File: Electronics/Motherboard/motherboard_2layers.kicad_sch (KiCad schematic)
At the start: 54 parts, among them J1 DX07S024JJ3R1300, J2 Conn_02x10_Odd_Even, M1 AO3400A, M2 AO3400A, M3 AO3400A, U1 AMS1117-3.3, U2 TMC2209_SILENTSTEPSTICK, U3 TMC2209_SILENTSTEPSTICK, U4 TMC2209_SILENTSTEPSTICK, U5 TMC2209_SILENTSTEPSTICK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

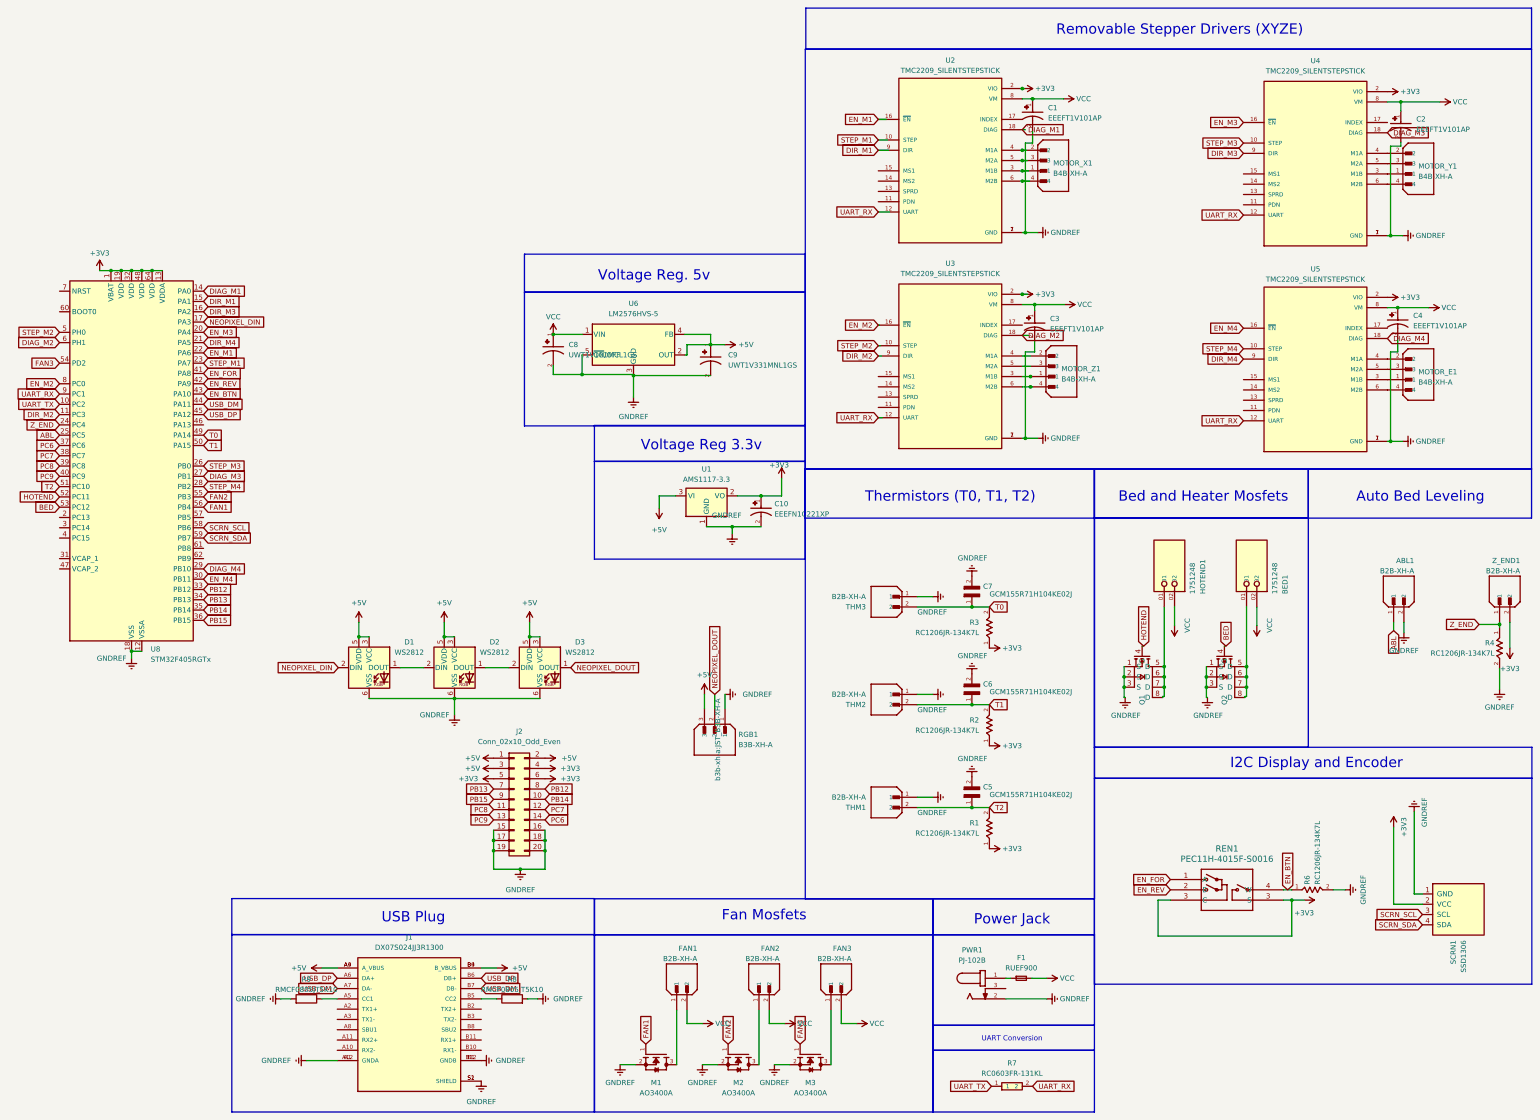
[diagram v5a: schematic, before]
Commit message: updated schmentic with proper values and updated usb c connector
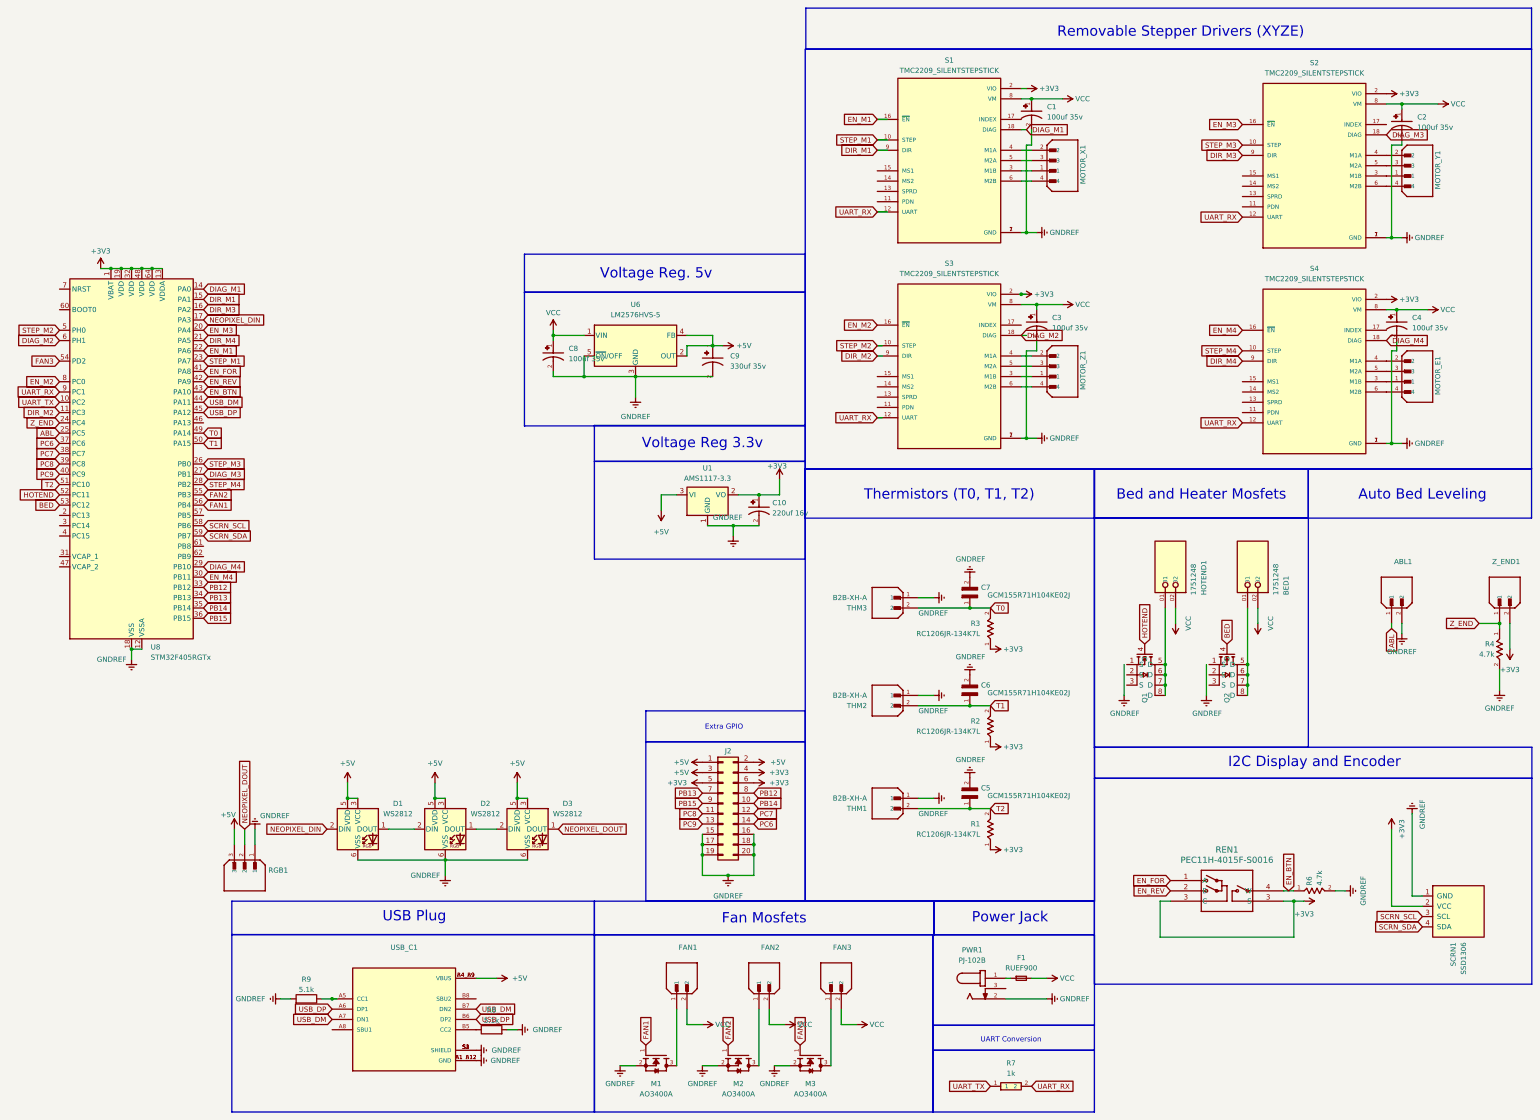
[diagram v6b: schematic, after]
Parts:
- removed C8: UWT1V101MCL1GS, UWT1V101MCL1GS:CAPAE830X1000N, symbol UWT1V101MCL1GS:UWT1V101MCL1GS
- removed J1: DX07S024JJ3R1300, DX07S024JJ3R1300:JAE_DX07S024JJ3R1300, symbol DX07S024JJ3R1300:DX07S024JJ3R1300
- added C8: 100uf 35v, CAP_EEEFT1V101AP, symbol EEEFT1V101AP:EEEFT1V101AP
- added USB_C1: TYPE-C-31-M-12, Connector_USB:USB_C_Receptacle_HRO_TYPE-C-31-M-12, symbol USB_C_Receptacle_HRO_TYPE:TYPE-C-31-M-12
- ABL1, FAN2, FAN3, Z_END1: Check_prices https://www.snapeda.com/parts/B2B-XH-A/JST+Sales+America+In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 -> (none); DigiKey_Part_Number 455-B2B-XH-A-ND -> (none); MANUFACTURER JST Sales America Inc. -> (none); MAXIMUM_PACKAGE_HEIGHT 7 mm -> (none); MF JST Sales -> (none); MP B2B-XH-A -> (none); PARTREV N/A -> (none); Package None -> (none); STANDARD Manufacturer Recommendations -> (none); SnapEDA_Link https://www.snapeda.com/parts/B2B-XH-A/JST+Sales+America+In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 -> (none)
- C1, C2, C3, C4: value EEEFT1V101AP -> 100uf 35v; Availability In Stock -> (none); Check_prices https://www.snapeda.com/parts/EEEFT1V101AP/Panasonic/view-p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 -> (none); Description_1 100µF 35V Aluminum Electrolytic Capacitors Radial, Can - SM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 -> (none); MANUFACTURER Panasonic -> (none); MAXIMUM_PACKAGE_HEIGHT 5.8mm -> (none); MF Panasonic -> (none); MP EEEFT1V101AP -> (none); PARTREV 10-Oct-19 -> (none); Package RADIAL-2 Panasonic -> (none); Price None -> (none); Purchase-URL https://www.snapeda.com/api/url_track_click_mouser/?unipart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 -> (none); STANDARD Manufacturer Recommendations -> (none); SnapEDA_Link https://www.snapeda.com/parts/EEEFT1V101AP/Panasonic/view-p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 -> (none)
- C10: value EEEFN1C221XP -> 220uf 16v; Availability In Stock -> (none); Check_prices https://www.snapeda.com/parts/EEE-FN1C221XP/Panasonic/view-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 -> (none); Description_1 Capacitor,16VDC, 220uF,SMD'Electrolytic | Panasonic Electro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 -> (none); MANUFACTURER Panasonic -> (none); MAXIMUM_PACKAGE_HEIGHT 7.7mm -> (none); MF Panasonic Electronic Components -> (none); MP EEE-FN1C221XP -> (none); PARTREV 10-Oct-19 -> (none); Package RADIAL-2 Panasonic -> (none); Price None -> (none); Purchase-URL https://www.snapeda.com/api/url_track_click_mouser/?unipart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 -> (none); STANDARD Manufacturer Recommendations -> (none); SnapEDA_Link https://www.snapeda.com/parts/EEE-FN1C221XP/Panasonic/view-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 -> (none)
- C9: value UWT1V331MNL1GS -> 330uf 35v; Availability In Stock -> (none); Check_prices https://www.snapeda.com/parts/UWT1V101MCL1GS/Nichicon/view-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 -> (none); Description_1 Capacitor Aluminum Electrolytic, 1000h 6.3 (Dia.) x 7.7mm, 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 -> (none); MANUFACTURER Nichicon -> (none); MAXIMUM_PACKAGE_HEIGHT 7.7mm -> (none); MF Nichicon -> (none); MP UWT1V101MCL1GS -> (none); PARTREV CAT.8100L -> (none); Package Radial Nichicon -> (none); Price None -> (none); Purchase-URL https://www.snapeda.com/api/url_track_click_mouser/?unipart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 -> (none); SNAPEDA_PN UWT1V101MCL1GS -> (none); STANDARD IPC-7351B -> (none); SnapEDA_Link https://www.snapeda.com/parts/UWT1V101MCL1GS/Nichicon/view-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 -> (none)
- FAN1: value B2B-XH-A -> ~
- MOTOR_E1, MOTOR_X1, MOTOR_Y1, MOTOR_Z1: Check_prices https://www.snapeda.com/parts/B4B-XH-A/JST+Sales+America+In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 -> (none); DigiKey_Part_Number 455-B4B-XH-A-ND -> (none); MANUFACTURER JST -> (none); MAXIMUM_PACKAGE_HEIGHT 7.00 mm -> (none); MF JST Sales -> (none); MP B4B-XH-A -> (none); PARTREV 7/4/21 -> (none); Package None -> (none); STANDARD Manufacturer Recommendations -> (none); SnapEDA_Link https://www.snapeda.com/parts/B4B-XH-A/JST+Sales+America+In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 -> (none)
- R4, R6: value RC1206JR-134K7L -> 4.7k; Check_prices https://www.snapeda.com/parts/RC1206JR-134K7L/Yageo/view-pa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 -> (none); DigiKey_Part_Number 13-RC1206JR-134K7LTR-ND -> (none); MANUFACTURER YAGEO -> (none); MF Yageo -> (none); MP RC1206JR-134K7L -> (none); Package SMD-2 Yageo -> (none); Purchase-URL https://www.snapeda.com/api/url_track_click_mouser/?unipart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 -> (none); SnapEDA_Link https://www.snapeda.com/parts/RC1206JR-134K7L/Yageo/view-pa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 -> (none)
- R7: value RC0603FR-131KL -> 1k; Check_prices https://www.snapeda.com/parts/RC0603FR-131KL/Yageo/view-par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 -> (none); DigiKey_Part_Number 13-RC0603FR-131KLTR-ND -> (none); MF Yageo -> (none); MP RC0603FR-131KL -> (none); Package 0603 Yageo -> (none); Purchase-URL https://www.snapeda.com/api/url_track_click_mouser/?unipart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 -> (none); SnapEDA_Link https://www.snapeda.com/parts/RC0603FR-131KL/Yageo/view-par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 -> (none)
- R8, R9: value RMCF0805JT5K10 -> 5.1k
- renumbered U2 to S1, U4 to S2, U3 to S3, U5 to S4
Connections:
- net +5V: now also USB_C1.A4_B9 (VBUS), USB_C1.B4_A9 (VBUS)
- net GNDREF: now also C8.2, USB_C1.A1_B12 (GND), USB_C1.B1_A12 (GND), USB_C1.S1 (SHIELD), USB_C1.S2 (SHIELD), USB_C1.S3 (SHIELD), USB_C1.S4 (SHIELD); no longer Q1.1 (S), Q1.2 (S), Q1.3 (S), Q2.1 (S), Q2.2 (S), Q2.3 (S)
- net USB_DM: now also USB_C1.A7 (DN1), USB_C1.B7 (DN2)
- net USB_DP: now also USB_C1.A6 (DP1), USB_C1.B6 (DP2)
- net VCC: now also C8.1
- net at R9.1: now also USB_C1.A5 (CC1)
- net at R8.1: now also USB_C1.B5 (CC2)
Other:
- note added: "Extra GPIO"
- moved on the sheet: ABL1, C10, C4, C5, C6, C7, C9, D1, D2, D3, J2, MOTOR_E1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

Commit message: more clean up neneds to be done
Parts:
- renumbered MOTOR_E1 to MOTOR_E, MOTOR_X1 to MOTOR_X, MOTOR_Y1 to MOTOR_Y, MOTOR_Z1 to MOTOR_Z
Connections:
- net GNDREF: now also Q1.1 (S), Q1.2 (S), Q1.3 (S), Q2.1 (S), Q2.2 (S), Q2.3 (S)
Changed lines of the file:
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@@
 	)
 	(junction
+		(at 328.295 179.07)
+		(diameter 0)
+		(color 0 0 0 0)
+	)
+	(junction
 		(at 203.2 218.44)
 		(diameter 0)
@@
 	)
 	(junction
+		(at 307.975 179.07)
+		(diameter 0)
+		(color 0 0 0 0)
+	)
+	(junction
 		(at 283.21 118.11)
 		(diameter 0)
@@
 	)
 	(junction
+		(at 307.975 176.53)
+		(diameter 0)
+		(color 0 0 0 0)
+	)
+	(junction
+		(at 328.295 176.53)
+		(diameter 0)
+		(color 0 0 0 0)
+	)
+	(junction
 		(at 349.25 232.41)
 		(diameter 0)
@@
 	(wire
 		(pts
+			(xy 307.34 179.07) (xy 307.975 179.07)
+		)
+		(stroke
+			(width 0)
+			(type default)
+		)
+	)
+	(wire
+		(pts
 			(xy 118.11 222.25) (xy 139.7 222.25)
 		)
@@
 	(wire
 		(pts
-			(xy 307.34 173.99) (xy 307.34 181.61)
-		)
-		(stroke
-			(width 0)
-			(type default)
-		)
-	)
-	(wire
-		(pts
 			(xy 283.21 96.52) (xy 283.21 118.11)
 		)
@@
 	(wire
 		(pts
-			(xy 327.66 173.99) (xy 327.66 181.61)
+			(xy 328.295 173.99) (xy 328.295 176.53)
 		)
 		(stroke
@@
 	(wire
 		(pts
+			(xy 328.295 179.07) (xy 327.66 179.07)
+		)
+		(stroke
+			(width 0)
+			(type default)
+		)
+	)
+	(wire
+		(pts
 			(xy 67.31 76.2) (xy 69.85 76.2)
 		)
@@
 	(wire
 		(pts
+			(xy 328.295 176.53) (xy 328.295 179.07)
+		)
+		(stroke
+			(width 0)
+			(type default)
+		)
+	)
+	(wire
+		(pts
 			(xy 203.2 262.89) (xy 199.39 262.89)
 		)
@@
 	(wire
 		(pts
+			(xy 307.975 176.53) (xy 307.975 179.07)
+		)
+		(stroke
+			(width 0)
+			(type default)
+		)
+	)
+	(wire
+		(pts
 			(xy 373.38 45.72) (xy 373.38 68.58)
 		)
@@
 	(wire
 		(pts
+			(xy 307.975 173.99) (xy 307.975 176.53)
+		)
+		(stroke
+			(width 0)
+			(type default)
+		)
+	)
+	(wire
+		(pts
 			(xy 375.92 35.56) (xy 384.81 35.56)
 		)
@@
 	(symbol
 		(lib_id "power:GNDREF")
-		(at 307.34 181.61 0)
+		(at 307.34 179.07 270)
 		(unit 1)
 		(exclude_from_sim no)
@@
 		(dnp no)
 		(property "Reference" "#PWR040"
-			(at 307.34 187.96 0)
+			(at 300.99 179.07 0)
 			(effects
 				(font
@@
 		)
 		(property "Value" "GNDREF"
-			(at 311.15 186.055 0)
+			(at 302.895 182.88 0)
 			(effects
 				(font
@@
 		)
 		(property "Footprint" ""
-			(at 307.34 181.61 0)
+			(at 307.34 179.07 0)
 			(effects
 				(font
@@
 		)
 		(property "Datasheet" ""
-			(at 307.34 181.61 0)
+			(at 307.34 179.07 0)
 			(effects
 				(font
@@
 		)
 		(property "Description" ""
-			(at 307.34 181.61 0)
+			(at 307.34 179.07 0)
 			(effects
 				(font
@@
 		(on_board yes)
 		(dnp no)
-		(property "Reference" "MOTOR_X1"
+		(property "Reference" "MOTOR_X"
 			(at 297.18 55.372 90)
 			(effects
@@
 			(project "motherboard_2layers"
 				(path "/9290e430-09f5-4a3f-8744-4071dceedc2e"
-					(reference "MOTOR_X1")
+					(reference "MOTOR_X")
 					(unit 1)
 				)
@@
 		(on_board yes)
 		(dnp no)
-		(property "Reference" "MOTOR_Z1"
+		(property "Reference" "MOTOR_Z"
 			(at 297.18 106.172 90)
 			(effects
@@
 			(project "motherboard_2layers"
 				(path "/9290e430-09f5-4a3f-8744-4071dceedc2e"
-					(reference "MOTOR_Z1")
+					(reference "MOTOR_Z")
 					(unit 1)
 				)
@@
 	(symbol
 		(lib_id "power:GNDREF")
-		(at 327.66 181.61 0)
+		(at 327.66 179.07 270)
 		(unit 1)
 		(exclude_from_sim no)
@@
 		(dnp no)
 		(property "Reference" "#PWR041"
-			(at 327.66 187.96 0)
+			(at 321.31 179.07 0)
 			(effects
 				(font
@@
 		)
 		(property "Value" "GNDREF"
-			(at 331.47 186.055 0)
+			(at 323.215 182.88 0)
 			(effects
 				(font
@@
 		)
 		(property "Footprint" ""
-			(at 327.66 181.61 0)
+			(at 327.66 179.07 0)
 			(effects
 				(font
@@
 		)
 		(property "Datasheet" ""
-			(at 327.66 181.61 0)
+			(at 327.66 179.07 0)
 			(effects
 				(font
@@
 		)
 		(property "Description" ""
-			(at 327.66 181.61 0)
+			(at 327.66 179.07 0)
 			(effects
 				(font
@@
 		(on_board yes)
 		(dnp no)
-		(property "Reference" "MOTOR_Y1"
+		(property "Reference" "MOTOR_Y"
 			(at 384.81 56.642 90)
 			(effects
@@
 			(project "motherboard_2layers"
 				(path "/9290e430-09f5-4a3f-8744-4071dceedc2e"
-					(reference "MOTOR_Y1")
+					(reference "MOTOR_Y")
 					(unit 1)
 				)
@@
 		(on_board yes)
 		(dnp no)
-		(property "Reference" "MOTOR_E1"
+		(property "Reference" "MOTOR_E"
 			(at 384.81 107.442 90)
 			(effects
@@
 			(project "Motherboard"
 				(path "/9290e430-09f5-4a3f-8744-4071dceedc2e"
-					(reference "MOTOR_E1")
+					(reference "MOTOR_E")
 					(unit 1)
 				)

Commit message: rahhhh i need some1 to look over this
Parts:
- renumbered MOTOR_E to MOTOR_E1, MOTOR_X to MOTOR_X1, MOTOR_Y to MOTOR_Y1, MOTOR_Z to MOTOR_Z1
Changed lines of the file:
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@@
 		(on_board yes)
 		(dnp no)
-		(property "Reference" "MOTOR_X"
+		(property "Reference" "MOTOR_X1"
 			(at 297.18 55.372 90)
 			(effects
@@
 			(project "motherboard_2layers"
 				(path "/9290e430-09f5-4a3f-8744-4071dceedc2e"
-					(reference "MOTOR_X")
+					(reference "MOTOR_X1")
 					(unit 1)
 				)
@@
 		(on_board yes)
 		(dnp no)
-		(property "Reference" "MOTOR_Z"
+		(property "Reference" "MOTOR_Z1"
 			(at 297.18 106.172 90)
 			(effects
@@
 			(project "motherboard_2layers"
 				(path "/9290e430-09f5-4a3f-8744-4071dceedc2e"
-					(reference "MOTOR_Z")
+					(reference "MOTOR_Z1")
 					(unit 1)
 				)
@@
 		(on_board yes)
 		(dnp no)
-		(property "Reference" "MOTOR_Y"
+		(property "Reference" "MOTOR_Y1"
 			(at 384.81 56.642 90)
 			(effects
@@
 			(project "motherboard_2layers"
 				(path "/9290e430-09f5-4a3f-8744-4071dceedc2e"
-					(reference "MOTOR_Y")
+					(reference "MOTOR_Y1")
 					(unit 1)
 				)
@@
 		(on_board yes)
 		(dnp no)
-		(property "Reference" "MOTOR_E"
+		(property "Reference" "MOTOR_E1"
 			(at 384.81 107.442 90)
 			(effects
@@
 			(project "Motherboard"
 				(path "/9290e430-09f5-4a3f-8744-4071dceedc2e"
-					(reference "MOTOR_E")
+					(reference "MOTOR_E1")
 					(unit 1)
 				)
